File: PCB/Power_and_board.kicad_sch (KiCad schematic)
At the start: 21 parts, among them U5 AMS1117-3.3

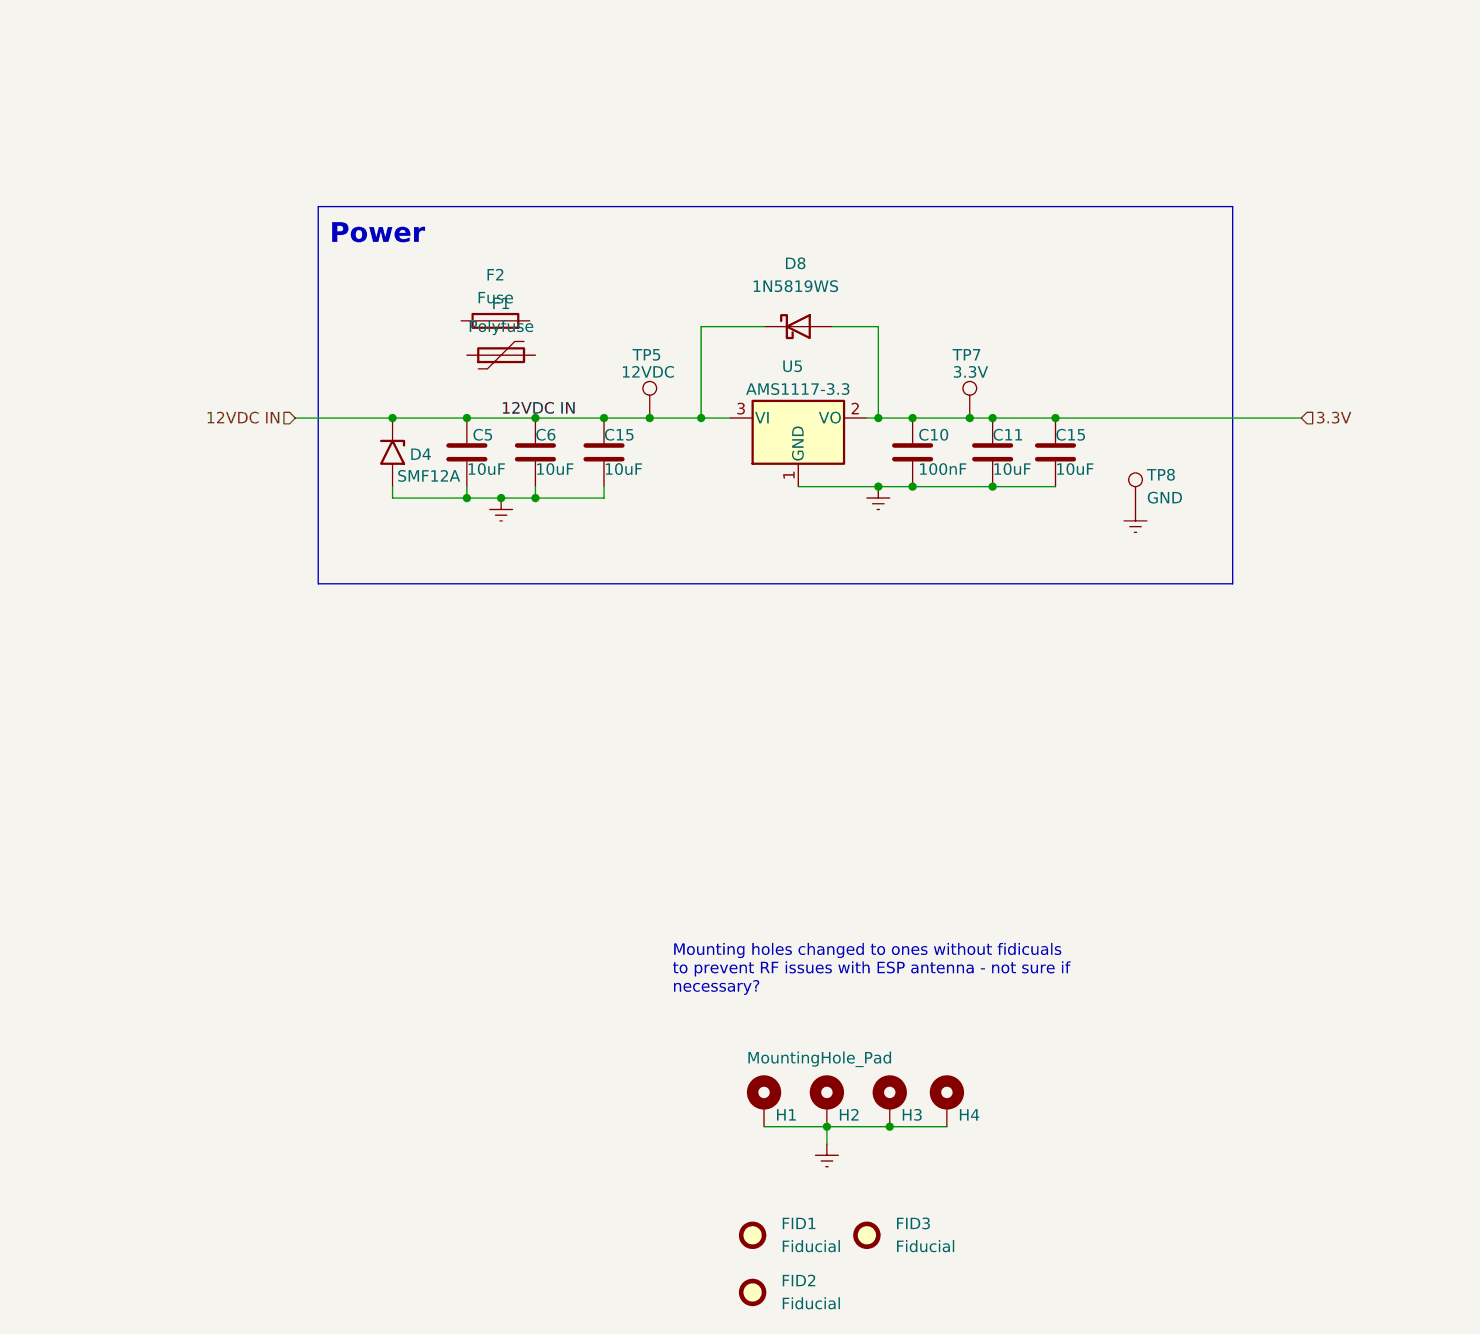
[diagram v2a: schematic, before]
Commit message: fuse added to schematic. began board re-layout
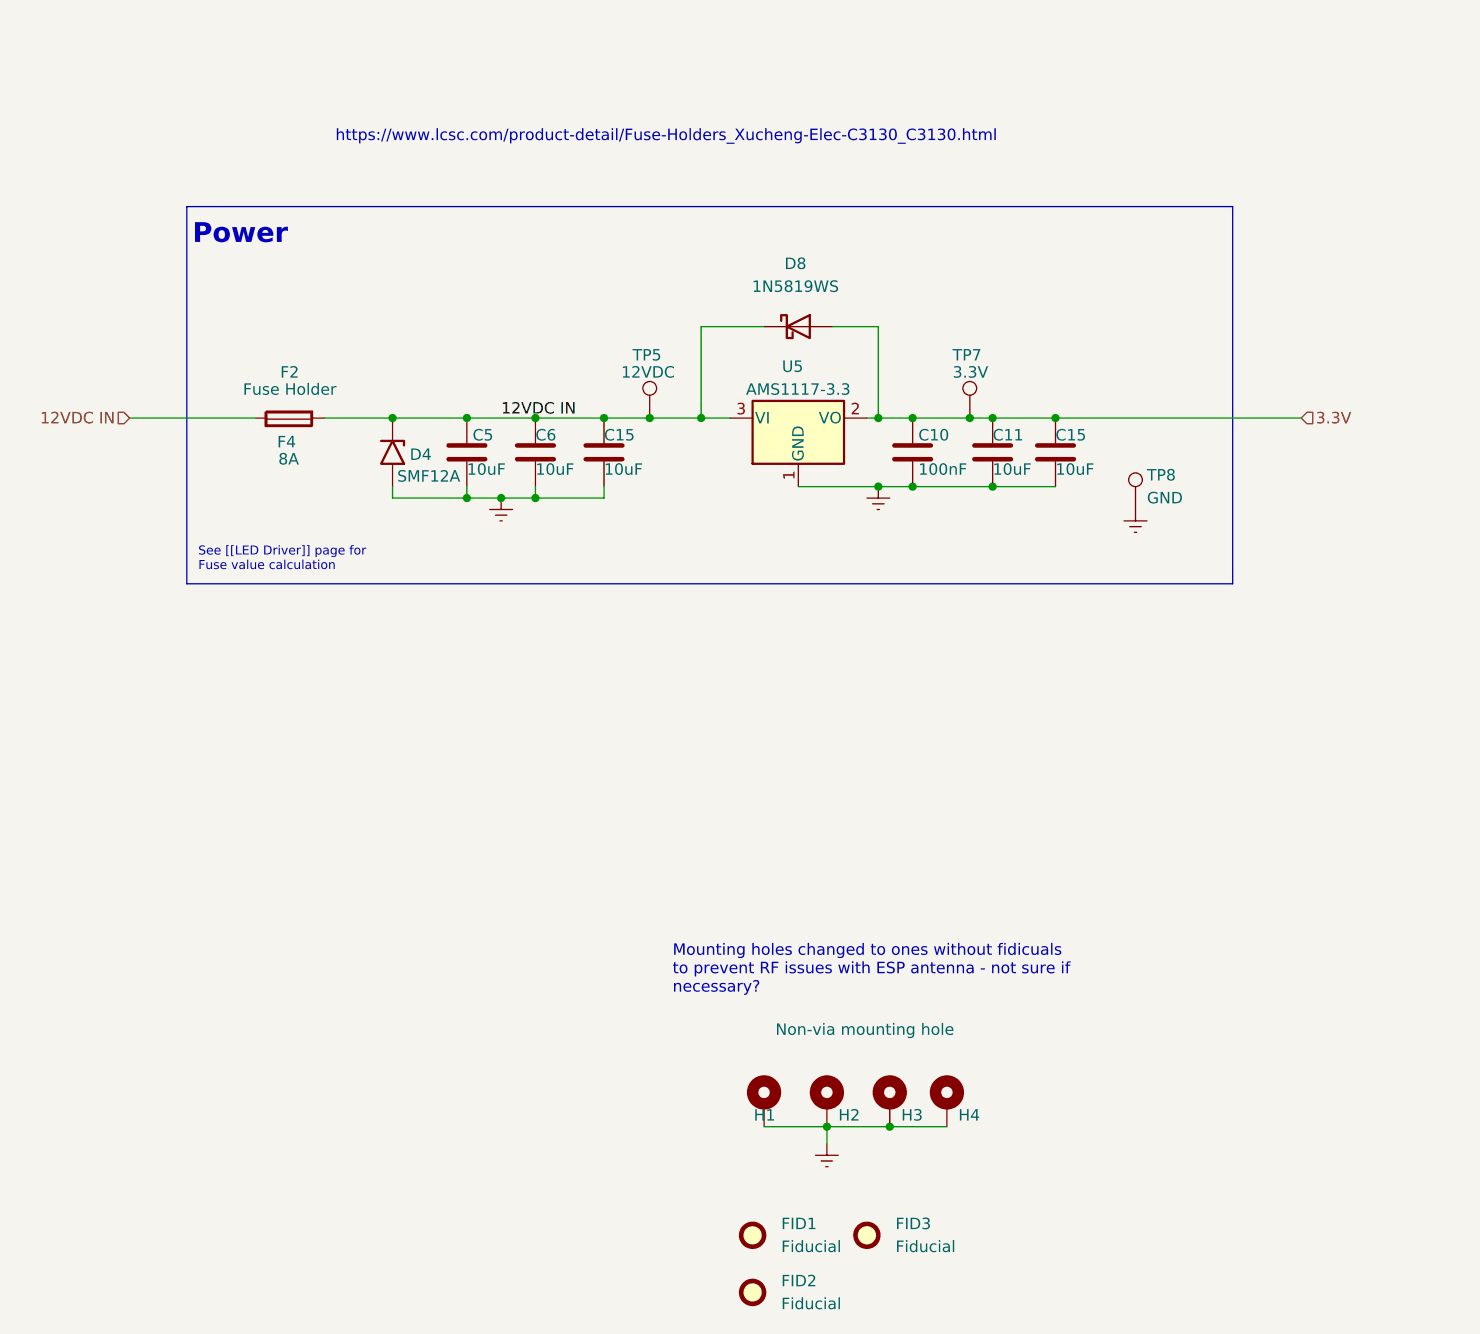
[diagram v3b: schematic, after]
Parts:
- removed F1: Polyfuse, symbol Device:Polyfuse
- removed F2: Fuse, symbol Device:Fuse
- added F2: Fuse Holder, Fuse:Fuseholder_Clip-5x20mm_Littelfuse_111_Inline_P20.00x5.00mm_D1.05mm_Horizontal, symbol projectlib:FuseHolder
- added F4: 8A, symbol projectlib:Fuse-noLegs
- H2: value MountingHole_Pad -> Non-via mounting hole
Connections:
- net 12VDC IN: now also F2.1, F2.2
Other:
- note added: "See [[LED Driver]] page for Fuse value calculation"
- note added: "https://www.lcsc.com/product-detail/Fuse-Holders_Xucheng-Elec-C3130_C3130.html"
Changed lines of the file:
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@@
     (stroke (width 0) (type default))
   )
-  (wire (pts (xy 99.06 94.615) (xy 109.855 94.615))
+  (wire (pts (xy 80.645 94.615) (xy 94.615 94.615))
     (stroke (width 0) (type default))
   )
@@
     (stroke (width 0) (type default))
   )
+  (wire (pts (xy 102.235 94.615) (xy 109.855 94.615))
+    (stroke (width 0) (type default))
+  )
   (wire (pts (xy 144.145 84.455) (xy 144.145 94.615))
     (stroke (width 0) (type default))
@@
     (fill (type none))
   )
-  (rectangle (start 101.6 71.12) (end 203.2 113.03)
+  (rectangle (start 86.995 71.12) (end 203.2 113.03)
     (stroke (width 0) (type default))
     (fill (type none))
   )
-  (text "Power\n" (at 102.87 75.565 0)
+  (text "See [[LED Driver]] page for \nFuse value calculation"
+    (at 88.265 111.76 0)
+    (effects (font (size 1 1)) (justify left bottom) (href "#2"))
+  )
+  (text "Power\n" (at 87.63 75.565 0)
     (effects (font (size 2.2 2.2) (thickness 0.44) bold) (justify left bottom))
   )
@@
     (effects (font (size 1.27 1.27)) (justify left bottom))
   )
+  (text "https://www.lcsc.com/product-detail/Fuse-Holders_Xucheng-Elec-C3130_C3130.html"
+    (at 103.505 64.135 0)
+    (effects (font (size 1.27 1.27)) (justify left bottom))
+  )
   (label "12VDC IN" (at 121.92 94.615 0) (fields_autoplaced)
     (effects (font (size 1.27 1.27)) (justify left bottom))
@@
     (effects (font (size 1.27 1.27)) (justify left))
   )
-  (hierarchical_label "12VDC IN" (shape input) (at 99.06 94.615 180) (fields_autoplaced)
+  (hierarchical_label "12VDC IN" (shape input) (at 80.645 94.615 180) (fields_autoplaced)
     (effects (font (size 1.27 1.27)) (justify right))
   )
@@
     )
   )
-  (symbol (lib_id "Device:Polyfuse") (at 121.92 87.63 90) (unit 1)
-    (in_bom yes) (on_board yes) (dnp no) (fields_autoplaced)
-    (property "Reference" "F1" (at 121.92 81.915 90)
-      (effects (font (size 1.27 1.27)))
-    )
-    (property "Value" "Polyfuse" (at 121.92 84.455 90)
-      (effects (font (size 1.27 1.27)))
-    )
-    (property "Footprint" "" (at 127 86.36 0)
-      (effects (font (size 1.27 1.27)) (justify left) hide)
-    )
-    (property "Datasheet" "~" (at 121.92 87.63 0)
-      (effects (font (size 1.27 1.27)) hide)
-    )
-    (property "Description" "I think this one? https://www.lcsc.com/product-detail/Resettable-Fuses_BOURNS-MF-MSMF075-2_C84140.html" (at 121.92 87.63 90)
-      (effects (font (size 1.27 1.27)) hide)
-    )
-    (pin "1")
-    (pin "2")
-    (instances
-      (project "dumb-led-driver"
-        (path "/b6358773-9a18-4eb2-bc1b-d38393a8df39/ff2d7abe-3ed9-4cf8-a089-c3975f855094"
-          (reference "F1") (unit 1)
-        )
-      )
-    )
-  )
   (symbol (lib_id "Mechanical:MountingHole_Pad") (at 171.45 170.815 0) (unit 1)
     (in_bom no) (on_board yes) (dnp no)
@@
     )
   )
+  (symbol (lib_id "projectlib:FuseHolder") (at 98.425 94.615 0) (unit 1)
+    (in_bom yes) (on_board yes) (dnp no)
+    (property "Reference" "F2" (at 98.425 89.535 0)
+      (effects (font (size 1.27 1.27)))
+    )
+    (property "Value" "Fuse Holder" (at 98.425 91.44 0)
+      (effects (font (size 1.27 1.27)))
+    )
+    (property "Footprint" "Fuse:Fuseholder_Clip-5x20mm_Littelfuse_111_Inline_P20.00x5.00mm_D1.05mm_Horizontal" (at 99.695 100.965 0)
+      (effects (font (size 1.27 1.27)) hide)
+    )
+    (property "Datasheet" "~" (at 98.425 94.615 90)
+      (effects (font (size 1.27 1.27)) hide)
+    )
+    (property "Description" "I think this one: https://www.lcsc.com/product-detail/Fuse-Holders_Xucheng-Elec-9A-520SW1G1_C2927393.html" (at 98.425 103.505 0)
+      (effects (font (size 1.27 1.27)) hide)
+    )
+    (property "LCSC" "C2927393" (at 104.775 89.535 0)
+      (effects (font (size 1.27 1.27)) hide)
+    )
+    (pin "1")
+    (pin "2")
+    (instances
+      (project "dumb-led-driver"
+        (path "/b6358773-9a18-4eb2-bc1b-d38393a8df39/ff2d7abe-3ed9-4cf8-a089-c3975f855094"
+          (reference "F2") (unit 1)
+        )
+      )
+    )
+  )
   (symbol (lib_id "Mechanical:MountingHole_Pad") (at 151.13 170.815 0) (unit 1)
     (in_bom no) (on_board yes) (dnp no)
     (property "Reference" "H1" (at 152.4 172.085 0)
-      (effects (font (size 1.27 1.27)) (justify left))
+      (effects (font (size 1.27 1.27)) (justify right))
     )
     (property "Value" "MountingHole_Pad" (at 149.225 165.735 0)
-      (effects (font (size 1.27 1.27)) (justify left))
+      (effects (font (size 1.27 1.27)) (justify left) hide)
     )
     (property "Footprint" "MountingHole:MountingHole_2.2mm_M2_Pad_Via" (at 151.13 170.815 0)
@@
     )
   )
-  (symbol (lib_id "Device:Fuse") (at 121.285 83.82 90) (unit 1)
-    (in_bom yes) (on_board yes) (dnp no) (fields_autoplaced)
-    (property "Reference" "F2" (at 121.285 78.74 90)
-      (effects (font (size 1.27 1.27)))
-    )
-    (property "Value" "Fuse" (at 121.285 81.28 90)
-      (effects (font (size 1.27 1.27)))
-    )
-    (property "Footprint" "" (at 121.285 85.598 90)
-      (effects (font (size 1.27 1.27)) hide)
-    )
-    (property "Datasheet" "~" (at 121.285 83.82 0)
-      (effects (font (size 1.27 1.27)) hide)
-    )
-    (pin "1")
-    (pin "2")
-    (instances
-      (project "dumb-led-driver"
-        (path "/b6358773-9a18-4eb2-bc1b-d38393a8df39/ff2d7abe-3ed9-4cf8-a089-c3975f855094"
-          (reference "F2") (unit 1)
-        )
-      )
-    )
-  )
   (symbol (lib_id "Connector:TestPoint") (at 192.405 104.775 0) (unit 1)
     (in_bom no) (on_board yes) (dnp no)
@@
     )
   )
+  (symbol (lib_name "Fuse-noLegs_1") (lib_id "projectlib:Fuse-noLegs") (at 98.298 94.742 90) (unit 1)
+    (in_bom yes) (on_board no) (dnp no)
+    (property "Reference" "F4" (at 97.028 97.282 90)
+      (effects (font (size 1.27 1.27)) (justify right))
+    )
+    (property "Value" "8A" (at 97.155 99.187 90)
+      (effects (font (size 1.27 1.27)) (justify right))
+    )
+    (property "Footprint" "" (at 98.298 96.52 90)
+      (effects (font (size 1.27 1.27)) hide)
+    )
+    (property "Datasheet" "~" (at 98.298 94.742 0)
+      (effects (font (size 1.27 1.27)) hide)
+    )
+    (property "Description" "" (at 98.298 97.282 90)
+      (effects (font (size 1.27 1.27)) hide)
+    )
+    (instances
+      (project "dumb-led-driver"
+        (path "/b6358773-9a18-4eb2-bc1b-d38393a8df39/ff2d7abe-3ed9-4cf8-a089-c3975f855094"
+          (reference "F4") (unit 1)
+        )
+      )
+    )
+  )
   (symbol (lib_id "Mechanical:Fiducial") (at 149.86 191.77 0) (unit 1)
     (in_bom no) (on_board yes) (dnp no) (fields_autoplaced)
@@
       (effects (font (size 1.27 1.27)) (justify left))
     )
-    (property "Value" "MountingHole_Pad" (at 154.94 163.83 0)
-      (effects (font (size 1.27 1.27)) (justify left) hide)
+    (property "Value" "Non-via mounting hole" (at 152.4 162.56 0)
+      (effects (font (size 1.27 1.27)) (justify left))
     )
     (property "Footprint" "MountingHole:MountingHole_2.2mm_M2_ISO7380" (at 158.115 170.815 0)

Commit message: began rev2 of layout. board size will have to be increased
- will need to make compomises regarding I/O, wont be able to make both power in and out fit on same short side :(
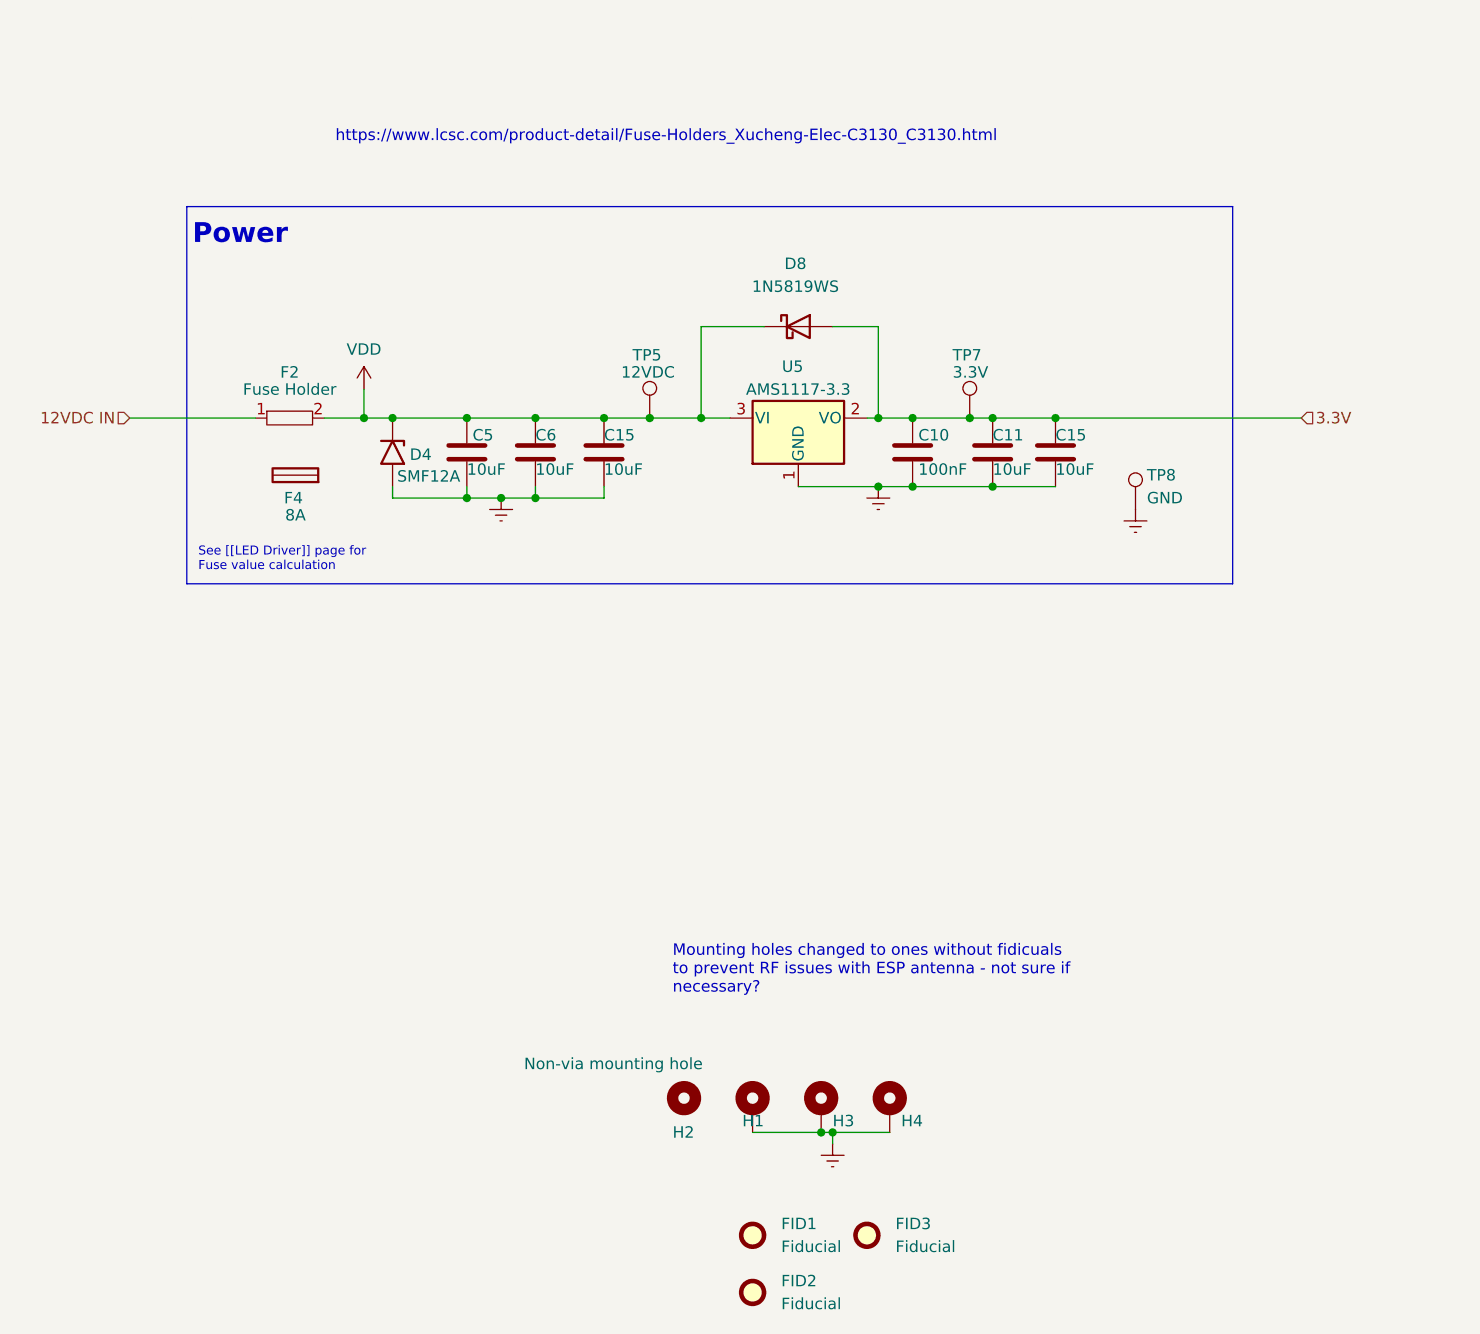
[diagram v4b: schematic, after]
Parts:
- H2: symbol Mechanical:MountingHole_Pad -> Mechanical:MountingHole
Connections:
- net 12VDC IN: no longer C15.1, C5.1, C6.1, D4.1 (A1), D8.1 (K), F2.2, TP5.1, U5.3 (VI)
- net Earth: no longer H2.1
- new net VDD: C15.1, C5.1, C6.1, D4.1 (A1), D8.1 (K), F2.2, TP5.1, U5.3 (VI)
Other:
- moved on the sheet: F4, H1, H3, H4
